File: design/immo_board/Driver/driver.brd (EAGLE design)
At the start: 160 x 100 mm, 24 parts, among them IC2 LM393N, IC3 74LS241N

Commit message: Add board for driver. Fix electric scheme.
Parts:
- removed JP10: +12V, pinhead:1X01
- removed JP8, JP9: +5V, pinhead:1X01
- added IC1, IC4, IC5, IC6, IC7: 7812TV, linear:TO220V
- added IC10, IC8, IC9: 7805TV, linear:TO220V
- added PAD1, PAD2, PAD3, PAD4: WIREPAD4,16O1,6, wirepad:4,16O1,6
- added PAD5, PAD6: (no value), wirepad:2,54/1,0
- added SV2: HC-SR04_right, con-lstb:MA04-1
- added SV3: HC-SR04_left, con-lstb:MA04-1
- moved SV1 506.1 mm to (52.8, 76.7)
- moved R13 422.0 mm to (119.1, 62.6)
- moved R12 406.6 mm to (119.1, 60.1), turned to 180 degrees
- moved IC3 405.5 mm to (115.9, 79.9), turned to 180 degrees
- moved IC2 373.5 mm to (132.3, 56.1)
- moved R9 304.5 mm to (118.0, 33.5), turned to 90 degrees
- moved R8 293.2 mm to (115.2, 36.0), turned to 90 degrees
- moved R7 281.9 mm to (112.2, 38.6), turned to 90 degrees
- moved R6 270.5 mm to (109.1, 41.2), turned to 90 degrees
- moved R5 269.7 mm to (128.9, 41.1)
- moved R4 258.7 mm to (125.7, 43.7)
- moved JP7 249.8 mm to (146.3, 67.2), turned to 359 degrees
- moved R1 248.6 mm to (131.6, 66.7)
- moved R3 247.8 mm to (122.8, 46.1)
- moved R2 237.1 mm to (119.9, 48.7)
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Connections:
- removed net GND1: U$1.P$21
- removed net N$24: JP1.2, JP10.1
- new net +12V: IC1.3, IC4.3, IC5.3, IC6.3, IC7.3, JP1.2
- new net +18V: IC1.1, IC10.1, IC4.1, IC5.1, IC6.1, IC7.1, IC8.1, IC9.1, PAD1.1, SV1.7
- new net +5V: IC10.3, IC2.8, IC3.20, IC8.3, IC9.3, JP4.2, JP5.2, JP7.2, R12.1, R13.2, SV1.8, SV2.4, SV3.4, U$1.P$18
- new net N$28: SV2.3, U$1.P$10
- new net N$29: SV2.2, U$1.P$11
- net GND: now also IC1.2, IC10.2, IC4.2, IC5.2, IC6.2, IC7.2, IC8.2, IC9.2, PAD3.1, PAD5.1, PAD6.1, SV2.1, SV3.1, U$1.P$21, U$1.P$22
- net N$14: now also U$1.P$31; no longer U$1.P$32
- net N$20: now also SV1.3; no longer SV1.2
- net N$21: now also SV1.2; no longer SV1.3
- net N$23: now also SV3.2, U$1.P$13; no longer IC2.8, JP4.2, JP5.2, JP7.2, JP8.1, R12.1, R13.2
- net N$25: now also SV3.3, U$1.P$12; no longer IC3.20, JP9.1, SV1.8, U$1.P$18
- net N$6: now also JP6.2; no longer JP6.3
- net N$7: now also JP6.3; no longer JP6.2
- net N$9: now also U$1.P$32; no longer U$1.P$31
- net VCC: now also PAD2.1, PAD4.1; no longer SV1.7
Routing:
- net GND: track 0.00 -> 878.9 mm
- net +5V: track 0.00 -> 347.6 mm
- net +18V: track 0.00 -> 312.8 mm
- net +12V: track 0.00 -> 201.3 mm
- net N$22: track 0.00 -> 59.8 mm
- net N$21: track 0.00 -> 59.3 mm
- net N$20: track 0.00 -> 56.7 mm
- net N$15: track 0.00 -> 53.3 mm
- net N$23: track 0.00 -> 52.0 mm
- net N$25: track 0.00 -> 51.7 mm
- net N$1: track 0.00 -> 42.4 mm
- net N$14: track 0.00 -> 40.1 mm
- net N$9: track 0.00 -> 37.7 mm
- net N$29: track 0.00 -> 36.8 mm
- net N$28: track 0.00 -> 36.4 mm
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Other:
- board size 160 x 100 mm -> 143.1 x 96 mm

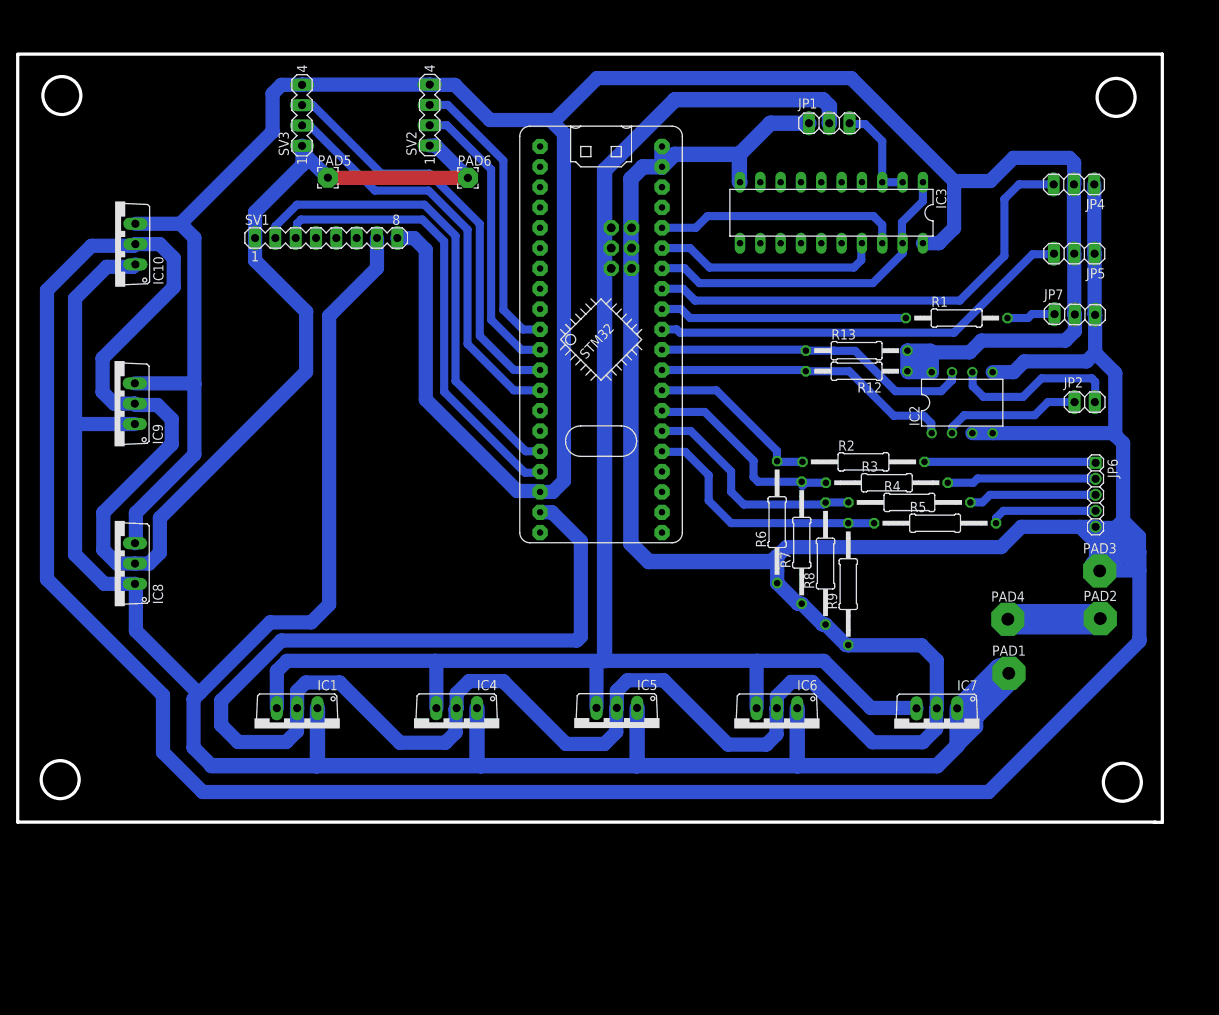
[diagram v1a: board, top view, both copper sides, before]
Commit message: Fix board for driver. Fix electric scheme.
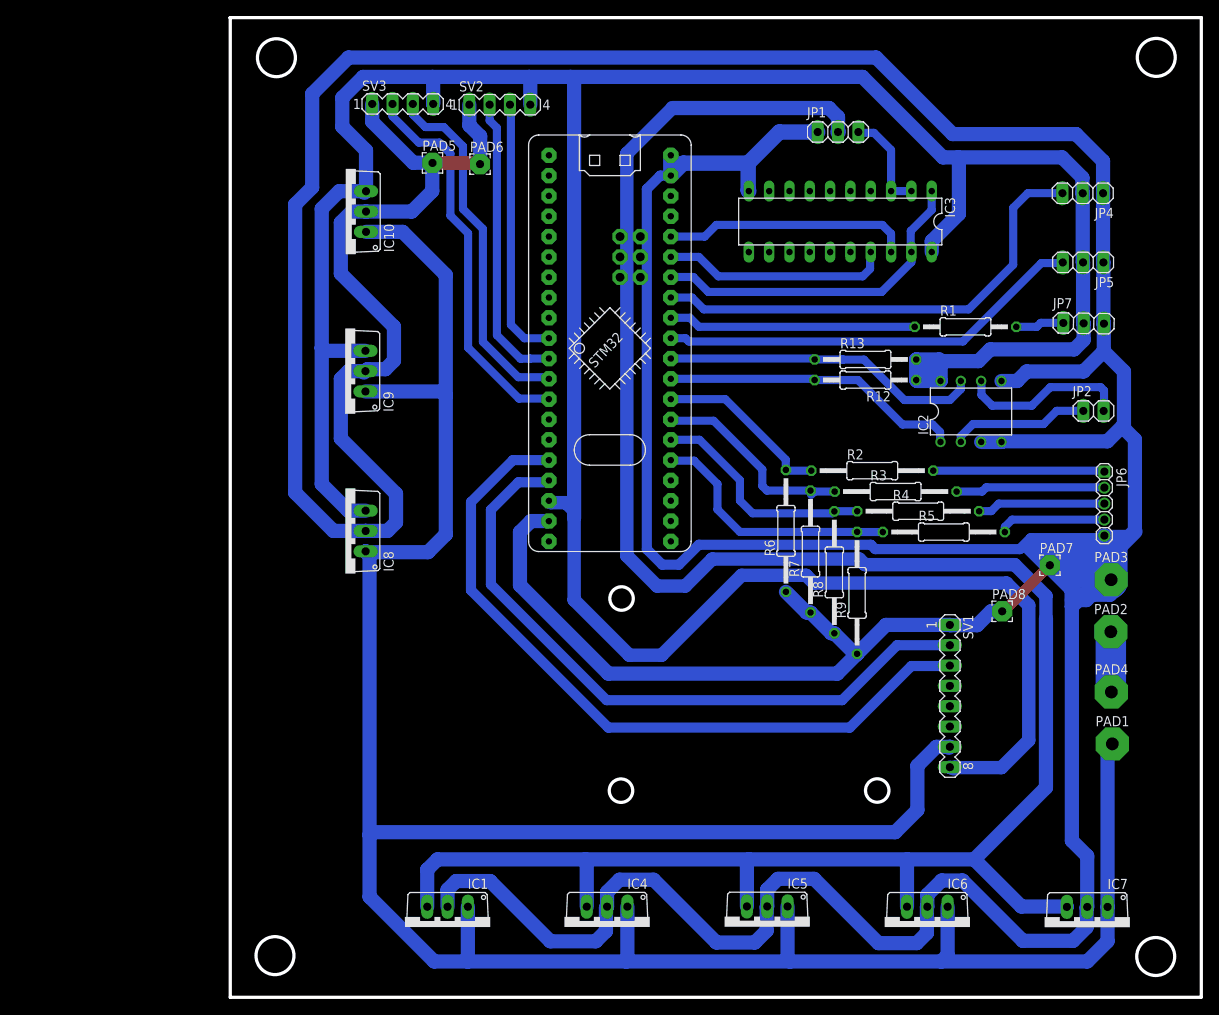
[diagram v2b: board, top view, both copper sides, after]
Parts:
- added PAD7, PAD8: (no value), wirepad:2,54/1,0
- moved SV1 96.7 mm to (130.7, 19.5), turned to 270 degrees
- moved IC4 31.1 mm to (87.9, -9.41)
- moved IC6 31.1 mm to (127.9, -9.42)
- moved IC1 31.1 mm to (67.9, -9.42)
- moved IC5 31.1 mm to (107.9, -9.38)
- moved IC7 31.1 mm to (147.9, -9.44)
- moved IC10 29.1 mm to (55.2, 80.0)
- moved IC9 29.1 mm to (55.1, 60.1)
- moved IC8 29.1 mm to (55.1, 40.1)
- moved PAD4 15.8 mm to (150.9, 20.0)
- moved PAD1 15.7 mm to (151.0, 13.5)
- moved PAD5 13.2 mm to (66.0, 86.1)
- moved SV3 12.7 mm to (62.3, 93.5), turned to 0 degrees
- moved SV2 8.86 mm to (74.5, 93.4), turned to 0 degrees
- moved PAD6 2.30 mm to (72.0, 86.0)
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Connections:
- net GND: now also PAD7.1, PAD8.1
- net N$20: now also SV1.2; no longer SV1.3
- net N$21: now also SV1.3; no longer SV1.2
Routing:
- net +12V: track 201.3 -> 281.1 mm
- net +5V: track 347.6 -> 405.6 mm
- net GND: track 878.9 -> 840.7 mm
- net N$21: track 59.3 -> 93.1 mm
- net N$20: track 56.7 -> 84.3 mm
- net +18V: track 312.8 -> 340.0 mm
- net N$25: track 51.7 -> 44.9 mm
- net VCC: track 11.6 -> 7.56 mm
- net N$28: track 36.4 -> 33.0 mm
- net N$23: track 52.0 -> 48.7 mm
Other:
- board size 143.1 x 96 mm -> 121.4 x 122.5 mm

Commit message: Fix board and electrical scheme for Encoder, Driver, WS2812B.
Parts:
- removed PAD5, PAD6, PAD7, PAD8: (no value), wirepad:2,54/1,0
- R1: value (none) -> 330 Om
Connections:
- net N$1 renamed P$27
- net N$10 renamed P$36
- net N$11 renamed P$35
- net N$12 renamed P$34
- net N$13 renamed P$33
- net N$14 renamed P$31
- net N$15 renamed P$30
- net N$18 renamed P$29
- net N$20 renamed P$17
- net N$21 renamed P$16
- net N$22 renamed P$28
- net N$23 renamed P$13
- net N$25 renamed P$12
- net N$28 renamed P$10
- net N$29 renamed P$11
- net N$3 renamed P$25
- net N$4 renamed P$26
- net N$9 renamed P$32
- net GND: no longer PAD5.1, PAD6.1, PAD7.1, PAD8.1
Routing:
- net GND: track 840.7 -> 784.7 mm, vias 0 -> 4
- net P$28: track 59.8 -> 55.3 mm
- net +5V: track 405.6 -> 409.4 mm
- net P$36: track 32.2 -> 30.3 mm
- net P$35: track 28.7 -> 27.0 mm
- net P$34: track 25.6 -> 24.2 mm
- net P$33: track 22.0 -> 21.3 mm
- net N$17: track 17.4 -> 18.2 mm
- net +18V: track 340.0 -> 339.4 mm

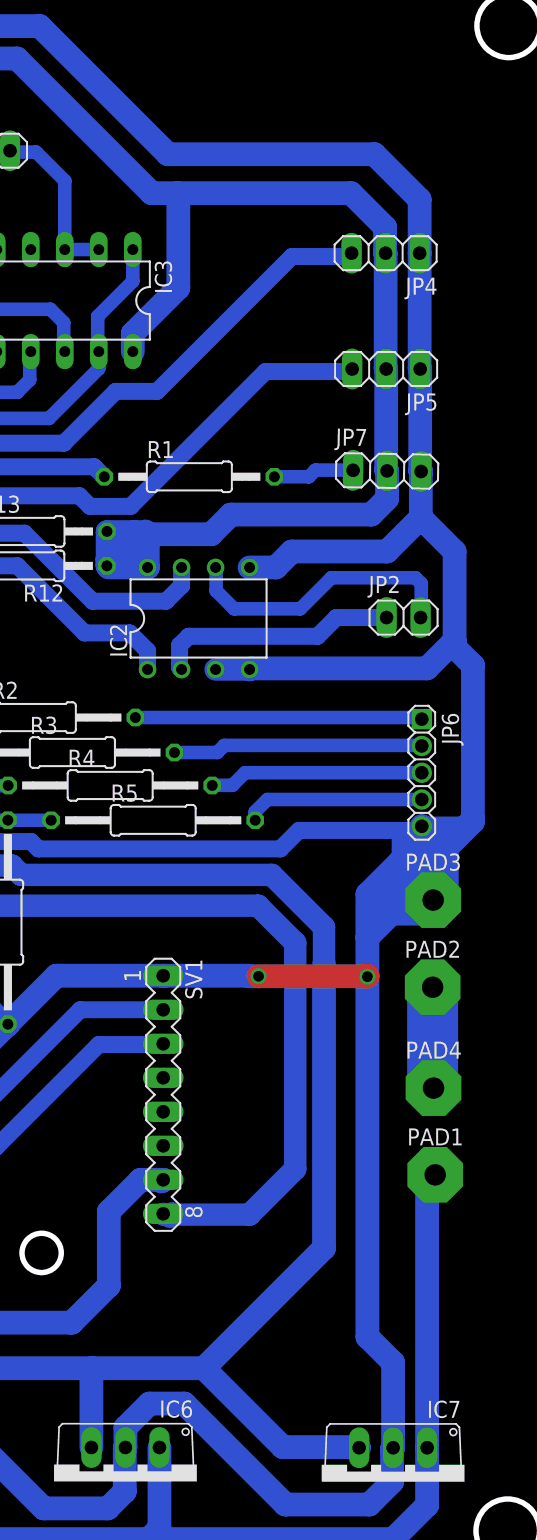
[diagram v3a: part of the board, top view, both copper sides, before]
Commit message: Fix board and electric scheme. Add capacitors.
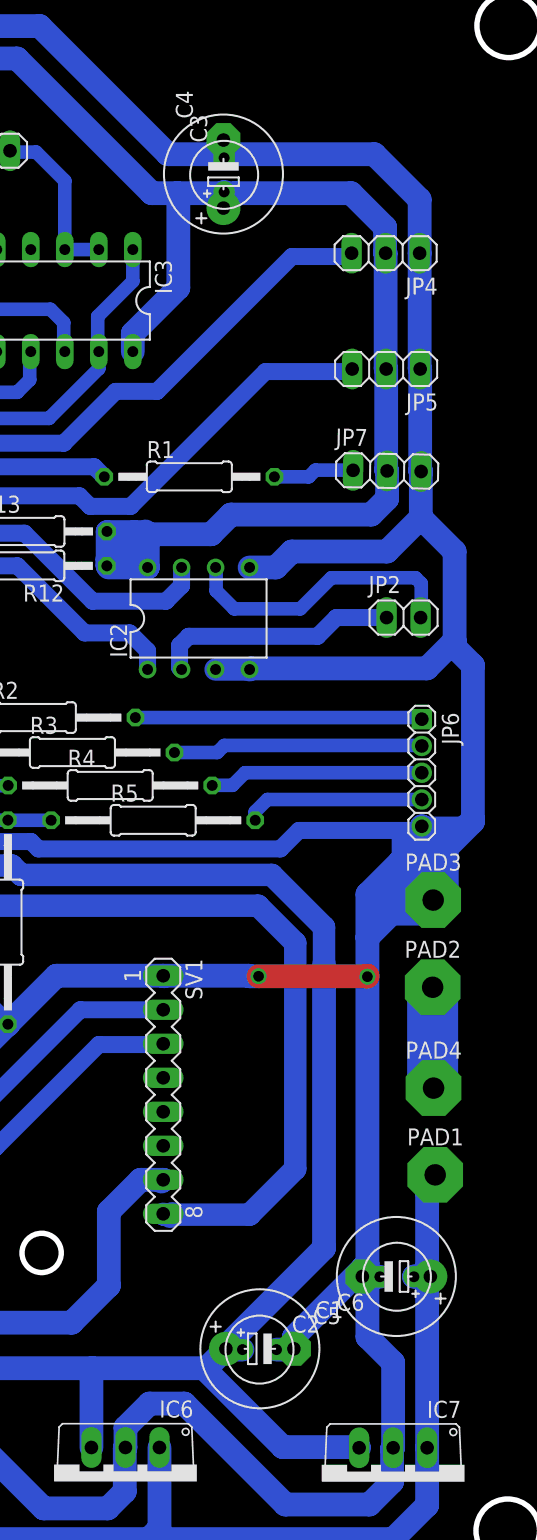
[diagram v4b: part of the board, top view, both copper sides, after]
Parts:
- added C1, C4, C5: (no value), resistor:E5-8,5
- added C2, C3, C6: (no value), resistor:E2,5-5
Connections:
- net +12V: now also C1.+, C2.+
- net +18V: now also C5.+, C6.+
- net +5V: now also C3.+, C4.+
- net GND: now also C1.-, C2.-, C3.-, C4.-, C5.-, C6.-
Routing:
- net GND: track 784.7 -> 800.5 mm
- net +18V: track 339.4 -> 343.4 mm
- net +5V: track 409.4 -> 411.8 mm
- net +12V: track 281.1 -> 282.5 mm
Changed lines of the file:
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@@
 <element name="PAD3" library="wirepad" package="4,16O1,6" value="WIREPAD4,16O1,6" x="150.88" y="34"/>
 <element name="PAD4" library="wirepad" package="4,16O1,6" value="WIREPAD4,16O1,6" x="150.91" y="19.96"/>
+<element name="C1" library="resistor" package="E5-8,5" value="" x="137.94" y="0.49"/>
+<element name="C2" library="resistor" package="E2,5-5" value="" x="137.91" y="0.43"/>
+<element name="C3" library="resistor" package="E2,5-5" value="" x="135.27" y="88.16" rot="R90"/>
+<element name="C4" library="resistor" package="E5-8,5" value="" x="135.22" y="88.22" rot="R90"/>
+<element name="C5" library="resistor" package="E5-8,5" value="" x="148.13" y="5.89" rot="R180"/>
+<element name="C6" library="resistor" package="E2,5-5" value="" x="148.17" y="5.87" rot="R180"/>
 </elements>
 <signals>
@@
 <wire x1="150.03" y1="38.5" x2="150.03" y2="39.51" width="1.778" layer="16"/>
 <wire x1="131.07" y1="89.7" x2="121.5" y2="99.27" width="1.778" layer="16"/>
-<wire x1="131.07" y1="89.7" x2="146.49" y2="89.7" width="1.778" layer="16"/>
+<wire x1="134.75" y1="89.7" x2="131.07" y2="89.7" width="1.778" layer="16"/>
+<wire x1="134.75" y1="89.7" x2="146.49" y2="89.7" width="1.778" layer="16"/>
 <wire x1="146.49" y1="89.7" x2="149.87" y2="86.32" width="1.778" layer="16"/>
 <wire x1="80.6" y1="41.33" x2="78.36" y2="41.33" width="1.778" layer="16"/>
@@
 <wire x1="147.89" y1="-6.9" x2="147.89" y2="-0.54" width="1.778" layer="16"/>
 <wire x1="147.89" y1="-0.54" x2="145.97" y2="1.38" width="1.778" layer="16"/>
-<wire x1="145.97" y1="1.38" x2="145.97" y2="28.28" width="1.778" layer="16"/>
+<wire x1="145.97" y1="5.14" x2="145.97" y2="1.38" width="1.778" layer="16"/>
+<wire x1="145.97" y1="6.86" x2="145.97" y2="5.14" width="1.778" layer="16"/>
+<wire x1="145.97" y1="6.86" x2="145.97" y2="28.28" width="1.778" layer="16"/>
 <wire x1="55.55" y1="99.27" x2="51.01" y2="94.73" width="1.778" layer="16"/>
 <wire x1="51.01" y1="94.73" x2="51.01" y2="83.04" width="1.778" layer="16"/>
@@
 <wire x1="65.4" y1="83.86" x2="65.4" y2="83.88" width="1.778" layer="1"/>
 <via x="65.4" y="83.88" extent="1-16" drill="0.8" diameter="1.016"/>
+<contactref element="C2" pad="-"/>
+<contactref element="C1" pad="-"/>
+<contactref element="C4" pad="-"/>
+<contactref element="C3" pad="-"/>
+<contactref element="C6" pad="-"/>
+<contactref element="C5" pad="-"/>
+<wire x1="145.97" y1="6.32" x2="145.97" y2="5.14" width="1.6764" layer="16"/>
+<wire x1="137.84" y1="28.31" x2="137.77" y2="28.31" width="1.6764" layer="16"/>
+<wire x1="139.18" y1="0.43" x2="140.42" y2="0.43" width="1.778" layer="16"/>
+<wire x1="140.42" y1="0.43" x2="140.48" y2="0.49" width="1.778" layer="16"/>
+<wire x1="140.48" y1="0.49" x2="140.48" y2="1.37" width="1.778" layer="16"/>
+<wire x1="140.48" y1="1.37" x2="145.59" y2="6.48" width="1.778" layer="16"/>
+<wire x1="146.9" y1="5.87" x2="145.61" y2="5.87" width="1.778" layer="16"/>
+<wire x1="145.61" y1="5.87" x2="145.59" y2="5.89" width="1.778" layer="16"/>
+<wire x1="145.59" y1="5.89" x2="145.59" y2="6.48" width="1.778" layer="16"/>
+<wire x1="145.59" y1="6.48" x2="145.97" y2="6.86" width="1.778" layer="16"/>
+<wire x1="135.27" y1="89.43" x2="135.27" y2="90.71" width="1.778" layer="16"/>
+<wire x1="135.27" y1="90.71" x2="135.22" y2="90.76" width="1.778" layer="16"/>
+<wire x1="135.22" y1="90.76" x2="135.22" y2="90.17" width="1.778" layer="16"/>
+<wire x1="135.22" y1="90.17" x2="134.75" y2="89.7" width="1.778" layer="16"/>
 <wire x1="57.68" y1="40.1" x2="57.69" y2="40.09" width="0" layer="19" extent="16-16"/>
 </signal>
@@
 <wire x1="130.44" y1="-6.88" x2="130.44" y2="-12.92" width="1.778" layer="16"/>
 <wire x1="130.44" y1="-12.92" x2="129.64" y2="-13.72" width="1.778" layer="16"/>
-<wire x1="150.43" y1="-6.9" x2="150.43" y2="13.16" width="1.778" layer="16"/>
+<wire x1="150.43" y1="6.64" x2="150.43" y2="-6.9" width="1.778" layer="16"/>
+<wire x1="150.43" y1="12.15" x2="150.43" y2="6.64" width="1.778" layer="16"/>
+<wire x1="150.43" y1="12.15" x2="150.43" y2="13.16" width="1.778" layer="16"/>
 <wire x1="150.43" y1="13.16" x2="151.33" y2="14.06" width="1.778" layer="16"/>
 <wire x1="130.72" y1="13.11" x2="129.03" y2="13.11" width="1.778" layer="16"/>
@@
 <wire x1="67.22" y1="57.53" x2="67.71" y2="57.04" width="1.778" layer="16"/>
 <contactref element="PAD1" pad="1"/>
-<wire x1="151.33" y1="14.06" x2="151.03" y2="13.48" width="0" layer="19" extent="16-16"/>
-<wire x1="57.8" y1="37.44" x2="58.18" y2="37.06" width="0" layer="19" extent="16-16"/>
+<contactref element="C5" pad="+"/>
+<contactref element="C6" pad="+"/>
+<wire x1="149.46" y1="5.89" x2="150.67" y2="5.89" width="1.778" layer="16"/>
+<wire x1="149.46" y1="5.89" x2="149.44" y2="5.87" width="1.778" layer="16"/>
+<wire x1="150.67" y1="5.89" x2="150.67" y2="6.4" width="1.778" layer="16"/>
+<wire x1="150.67" y1="6.4" x2="150.43" y2="6.64" width="1.778" layer="16"/>
+<wire x1="151.03" y1="13.48" x2="151.03" y2="13.05" width="1.778" layer="16"/>
+<wire x1="151.03" y1="13.05" x2="151.33" y2="12.75" width="1.778" layer="16"/>
+<wire x1="151.33" y1="12.75" x2="151.03" y2="12.75" width="1.778" layer="16"/>
+<wire x1="151.03" y1="12.75" x2="150.43" y2="12.15" width="1.778" layer="16"/>
+<wire x1="58.18" y1="37.06" x2="57.8" y2="37.44" width="0" layer="19" extent="16-16"/>
 </signal>
 <signal name="+5V">
@@
 <wire x1="119.8" y1="96.85" x2="129.86" y2="86.79" width="1.778" layer="16"/>
 <wire x1="131.78" y1="86.79" x2="129.86" y2="86.79" width="1.778" layer="16"/>
-<wire x1="131.78" y1="86.79" x2="144.75" y2="86.79" width="1.778" layer="16"/>
+<wire x1="136.15" y1="86.79" x2="131.78" y2="86.79" width="1.778" layer="16"/>
+<wire x1="136.15" y1="86.79" x2="144.75" y2="86.79" width="1.778" layer="16"/>
 <wire x1="144.75" y1="86.79" x2="147.29" y2="84.25" width="1.778" layer="16"/>
 <wire x1="147.29" y1="84.25" x2="147.29" y2="82.35" width="1.778" layer="16"/>
@@
 <wire x1="128.56" y1="61.53" x2="129.4" y2="61.53" width="1.6764" layer="16"/>
 <wire x1="128.56" y1="61.53" x2="126.52" y2="61.53" width="1.6764" layer="16"/>
-<wire x1="129.4" y1="61.53" x2="129.61" y2="61.32" width="1.6764" layer="16"/>
 <wire x1="126.52" y1="61.53" x2="126.52" y2="58.97" width="1.6764" layer="16"/>
 <wire x1="126.52" y1="58.97" x2="126.51" y2="58.96" width="1.6764" layer="16"/>
@@
 <wire x1="128.31" y1="59.37" x2="129.06" y2="59.37" width="1.6764" layer="16"/>
 <wire x1="129.06" y1="59.37" x2="129.57" y2="58.86" width="1.6764" layer="16"/>
+<contactref element="C3" pad="+"/>
+<contactref element="C4" pad="+"/>
+<wire x1="135.22" y1="86.84" x2="135.22" y2="85.68" width="1.778" layer="16"/>
+<wire x1="135.22" y1="86.84" x2="135.27" y2="86.89" width="1.778" layer="16"/>
+<wire x1="135.22" y1="85.68" x2="135.22" y2="85.86" width="1.778" layer="16"/>
+<wire x1="135.22" y1="85.86" x2="136.15" y2="86.79" width="1.778" layer="16"/>
 <wire x1="130.78" y1="10.51" x2="131.23" y2="10.4" width="0" layer="19" extent="16-16"/>
 </signal>
@@
 <wire x1="85.17" y1="-0.96" x2="105.6" y2="-0.96" width="1.778" layer="16"/>
 <wire x1="85.17" y1="-0.96" x2="66.67" y2="-0.96" width="1.778" layer="16"/>
-<wire x1="133.76" y1="-0.96" x2="125.42" y2="-0.96" width="1.778" layer="16"/>
+<wire x1="125.42" y1="-0.96" x2="133.76" y2="-0.96" width="1.778" layer="16"/>
 <wire x1="133.76" y1="-0.96" x2="139.65" y2="-6.85" width="1.778" layer="16"/>
 <wire x1="139.65" y1="-6.85" x2="145.3" y2="-6.85" width="1.778" layer="16"/>
@@
 <wire x1="116.77" y1="89.99" x2="116.74" y2="89.96" width="1.9304" layer="16"/>
 <wire x1="142.73" y1="8.01" x2="142.73" y2="29.19" width="1.778" layer="16"/>
-<wire x1="142.73" y1="8.01" x2="133.76" y2="-0.96" width="1.778" layer="16"/>
 <wire x1="116.74" y1="89.96" x2="116.74" y2="91.83" width="1.778" layer="16"/>
 <wire x1="116.74" y1="91.83" x2="115.61" y2="92.96" width="1.778" layer="16"/>
@@
 <wire x1="119.41" y1="36.58" x2="120.11" y2="35.88" width="1.6764" layer="16"/>
 <wire x1="94.12" y1="33.21" x2="97.65" y2="33.21" width="1.6764" layer="16"/>
+<contactref element="C2" pad="+"/>
+<contactref element="C1" pad="+"/>
+<wire x1="136.64" y1="0.43" x2="135.4" y2="0.43" width="1.778" layer="16"/>
+<wire x1="135.4" y1="0.43" x2="135.4" y2="0.49" width="1.778" layer="16"/>
+<wire x1="133.76" y1="-0.96" x2="133.95" y2="-0.96" width="1.778" layer="16"/>
+<wire x1="133.95" y1="-0.96" x2="135.4" y2="0.49" width="1.778" layer="16"/>
+<wire x1="135.4" y1="0.49" x2="135.4" y2="0.68" width="1.778" layer="16"/>
+<wire x1="135.4" y1="0.68" x2="142.73" y2="8.01" width="1.778" layer="16"/>
 </signal>
 <signal name="VCC">
